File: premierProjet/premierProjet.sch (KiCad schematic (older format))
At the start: 4 parts, among them J1 Conn_01x02_Male, SW1 Pushbutton

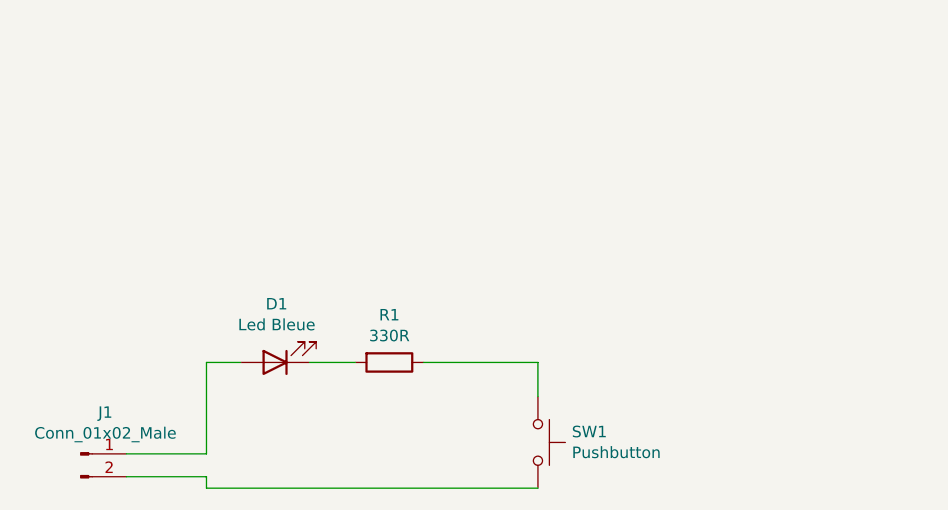
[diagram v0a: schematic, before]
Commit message: Added docs+ /docs
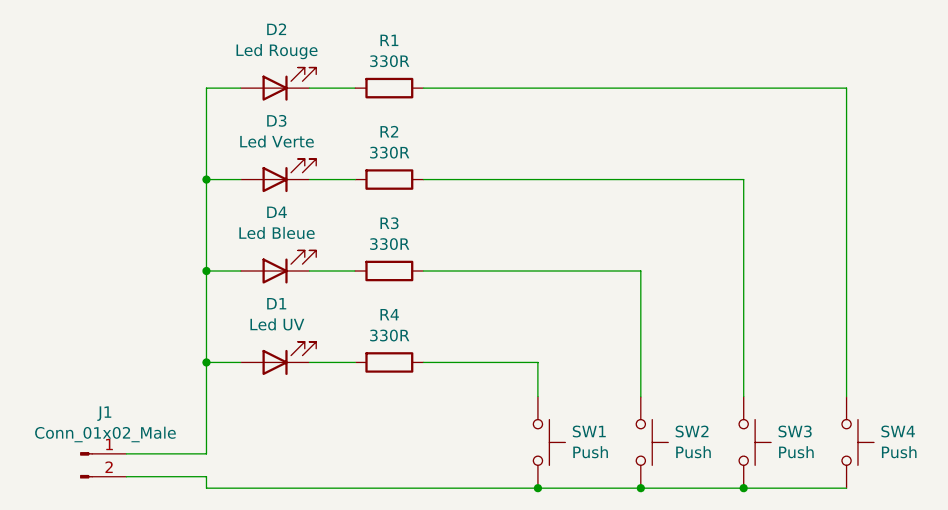
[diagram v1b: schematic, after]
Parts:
- added D2: Led Rouge, symbol Device:LED
- added D3: Led Verte, symbol Device:LED
- added D4: Led Bleue, symbol Device:LED
- added R1, R2, R3: 330R, symbol Device:R
- added SW2, SW3, SW4: Push, symbol Switch:SW_Push
- D1: value Led Bleue -> Led UV
- SW1: value Pushbutton -> Push
- renumbered R1 to R4
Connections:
- net at D1.2 (A), J1.1 (Pin_1): now also D2.2 (A), D3.2 (A), D4.2 (A)
- net at J1.2 (Pin_2), SW1.2: now also SW2.2, SW3.2, SW4.2
- new net: D4.1 (K), R3.2
- new net: R3.1, SW2.1
- new net: D3.1 (K), R2.2
- new net: R2.1, SW3.1
- new net: D2.1 (K), R1.2
- new net: R1.1, SW4.1
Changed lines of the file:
@@
 P 4350 3500
 F 0 "D1" H 4343 3245 50  0000 C CNN
-F 1 "Led Bleue" H 4343 3336 50  0000 C CNN
+F 1 "Led UV" H 4343 3336 50  0000 C CNN
 F 2 "" H 4350 3500 50  0001 C CNN
 F 3 "~" H 4350 3500 50  0001 C CNN
@@
 $EndComp
 $Comp
-L Device:R R1
+L Device:R R4
 U 1 1 5EB78021
 P 4850 3500
-F 0 "R1" V 4643 3500 50  0000 C CNN
+F 0 "R4" V 4643 3500 50  0000 C CNN
 F 1 "330R" V 4734 3500 50  0000 C CNN
 F 2 "" V 4780 3500 50  0001 C CNN
@@
 P 5500 3850
 F 0 "SW1" V 5454 3998 50  0000 L CNN
-F 1 "Pushbutton" V 5545 3998 50  0000 L CNN
+F 1 "Push" V 5545 3998 50  0000 L CNN
 F 2 "" H 5500 4050 50  0001 C CNN
 F 3 "~" H 5500 4050 50  0001 C CNN
@@
 Wire Wire Line
 	4050 4000 3700 4000
+$Comp
+L Device:LED D4
+U 1 1 5EB6F771
+P 4350 3100
+F 0 "D4" H 4343 2845 50  0000 C CNN
+F 1 "Led Bleue" H 4343 2936 50  0000 C CNN
+F 2 "" H 4350 3100 50  0001 C CNN
+F 3 "~" H 4350 3100 50  0001 C CNN
+	1    4350 3100
+	-1   0    0    1
+$EndComp
+$Comp
+L Device:R R3
+U 1 1 5EB6F777
+P 4850 3100
+F 0 "R3" V 4643 3100 50  0000 C CNN
+F 1 "330R" V 4734 3100 50  0000 C CNN
+F 2 "" V 4780 3100 50  0001 C CNN
+F 3 "~" H 4850 3100 50  0001 C CNN
+	1    4850 3100
+	0    1    1    0
+$EndComp
+Wire Wire Line
+	4050 3500 4050 3100
+Wire Wire Line
+	4050 3100 4200 3100
+Wire Wire Line
+	4500 3100 4700 3100
+$Comp
+L Device:LED D3
+U 1 1 5EB70A7C
+P 4350 2700
+F 0 "D3" H 4343 2445 50  0000 C CNN
+F 1 "Led Verte" H 4343 2536 50  0000 C CNN
+F 2 "" H 4350 2700 50  0001 C CNN
+F 3 "~" H 4350 2700 50  0001 C CNN
+	1    4350 2700
+	-1   0    0    1
+$EndComp
+$Comp
+L Device:R R2
+U 1 1 5EB70A82
+P 4850 2700
+F 0 "R2" V 4643 2700 50  0000 C CNN
+F 1 "330R" V 4734 2700 50  0000 C CNN
+F 2 "" V 4780 2700 50  0001 C CNN
+F 3 "~" H 4850 2700 50  0001 C CNN
+	1    4850 2700
+	0    1    1    0
+$EndComp
+Wire Wire Line
+	4050 3100 4050 2700
+Wire Wire Line
+	4050 2700 4200 2700
+Wire Wire Line
+	4500 2700 4700 2700
+$Comp
+L Device:LED D2
+U 1 1 5EB71F2C
+P 4350 2300
+F 0 "D2" H 4343 2045 50  0000 C CNN
+F 1 "Led Rouge" H 4343 2136 50  0000 C CNN
+F 2 "" H 4350 2300 50  0001 C CNN
+F 3 "~" H 4350 2300 50  0001 C CNN
+	1    4350 2300
+	-1   0    0    1
+$EndComp
+$Comp
+L Device:R R1
+U 1 1 5EB71F32
+P 4850 2300
+F 0 "R1" V 4643 2300 50  0000 C CNN
+F 1 "330R" V 4734 2300 50  0000 C CNN
+F 2 "" V 4780 2300 50  0001 C CNN
+F 3 "~" H 4850 2300 50  0001 C CNN
+	1    4850 2300
+	0    1    1    0
+$EndComp
+Wire Wire Line
+	4050 2700 4050 2300
+Wire Wire Line
+	4050 2300 4200 2300
+Wire Wire Line
+	4500 2300 4700 2300
+$Comp
+L Switch:SW_Push SW2
+U 1 1 5EB72A41
+P 5950 3850
+F 0 "SW2" V 5904 3998 50  0000 L CNN
+F 1 "Push" V 5995 3998 50  0000 L CNN
+F 2 "" H 5950 4050 50  0001 C CNN
+F 3 "~" H 5950 4050 50  0001 C CNN
+	1    5950 3850
+	0    1    1    0
+$EndComp
+$Comp
+L Switch:SW_Push SW3
+U 1 1 5EB733F4
+P 6400 3850
+F 0 "SW3" V 6354 3998 50  0000 L CNN
+F 1 "Push" V 6445 3998 50  0000 L CNN
+F 2 "" H 6400 4050 50  0001 C CNN
+F 3 "~" H 6400 4050 50  0001 C CNN
+	1    6400 3850
+	0    1    1    0
+$EndComp
+$Comp
+L Switch:SW_Push SW4
+U 1 1 5EB7399B
+P 6850 3850
+F 0 "SW4" V 6804 3998 50  0000 L CNN
+F 1 "Push" V 6895 3998 50  0000 L CNN
+F 2 "" H 6850 4050 50  0001 C CNN
+F 3 "~" H 6850 4050 50  0001 C CNN
+	1    6850 3850
+	0    1    1    0
+$EndComp
+Wire Wire Line
+	5500 4050 5950 4050
+Connection ~ 5500 4050
+Connection ~ 5950 4050
+Wire Wire Line
+	5950 4050 6400 4050
+Connection ~ 6400 4050
+Wire Wire Line
+	6400 4050 6850 4050
+Wire Wire Line
+	5000 3100 5950 3100
+Wire Wire Line
+	5950 3100 5950 3650
+Wire Wire Line
+	5000 2700 6400 2700
+Wire Wire Line
+	6400 2700 6400 3650
+Wire Wire Line
+	5000 2300 6850 2300
+Wire Wire Line
+	6850 2300 6850 3650
+Connection ~ 4050 3500
+Connection ~ 4050 3100
+Connection ~ 4050 2700
 $EndSCHEMATC

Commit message: PCB du prmierProjet
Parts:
- D1, D3: footprint (none) -> LED_SMD:LED_0805_2012Metric_Pad1.15x1.40mm_HandSolder
- D2: renamed from D4; footprint (none) -> LED_SMD:LED_0805_2012Metric_Pad1.15x1.40mm_HandSolder
- D4: renamed from D2; footprint (none) -> LED_SMD:LED_0805_2012Metric_Pad1.15x1.40mm_HandSolder
- J1: footprint (none) -> Connector_PinHeader_2.54mm:PinHeader_1x02_P2.54mm_Horizontal
- R1: renamed from R4; footprint (none) -> Resistor_SMD:R_0805_2012Metric_Pad1.15x1.40mm_HandSolder
- R2: renamed from R3; footprint (none) -> Resistor_SMD:R_0805_2012Metric_Pad1.15x1.40mm_HandSolder
- R3: renamed from R2; footprint (none) -> Resistor_SMD:R_0805_2012Metric_Pad1.15x1.40mm_HandSolder
- R4: renamed from R1; footprint (none) -> Resistor_SMD:R_0805_2012Metric_Pad1.15x1.40mm_HandSolder
- SW1, SW2, SW3, SW4: footprint (none) -> Button_Switch_THT:SW_PUSH_6mm
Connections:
- net Plus: now reaches D1.2 (A), D2.2 (A), D3.2 (A), D4.2 (A), J1.1 (Pin_1)
- net Masse: now reaches J1.2 (Pin_2), SW1.2, SW2.2, SW3.2, SW4.2
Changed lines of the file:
@@
 F 0 "D1" H 4343 3245 50  0000 C CNN
 F 1 "Led UV" H 4343 3336 50  0000 C CNN
-F 2 "" H 4350 3500 50  0001 C CNN
+F 2 "LED_SMD:LED_0805_2012Metric_Pad1.15x1.40mm_HandSolder" H 4350 3500 50  0001 C CNN
 F 3 "~" H 4350 3500 50  0001 C CNN
 	1    4350 3500
@@
 $EndComp
 $Comp
-L Device:R R4
+L Device:R R1
 U 1 1 5EB78021
 P 4850 3500
-F 0 "R4" V 4643 3500 50  0000 C CNN
+F 0 "R1" V 4643 3500 50  0000 C CNN
 F 1 "330R" V 4734 3500 50  0000 C CNN
-F 2 "" V 4780 3500 50  0001 C CNN
+F 2 "Resistor_SMD:R_0805_2012Metric_Pad1.15x1.40mm_HandSolder" V 4780 3500 50  0001 C CNN
 F 3 "~" H 4850 3500 50  0001 C CNN
 	1    4850 3500
@@
 F 0 "J1" H 3608 4081 50  0000 C CNN
 F 1 "Conn_01x02_Male" H 3608 3990 50  0000 C CNN
-F 2 "" H 3500 3900 50  0001 C CNN
+F 2 "Connector_PinHeader_2.54mm:PinHeader_1x02_P2.54mm_Horizontal" H 3500 3900 50  0001 C CNN
 F 3 "~" H 3500 3900 50  0001 C CNN
 	1    3500 3900
@@
 F 0 "SW1" V 5454 3998 50  0000 L CNN
 F 1 "Push" V 5545 3998 50  0000 L CNN
-F 2 "" H 5500 4050 50  0001 C CNN
+F 2 "Button_Switch_THT:SW_PUSH_6mm" H 5500 4050 50  0001 C CNN
 F 3 "~" H 5500 4050 50  0001 C CNN
 	1    5500 3850
@@
 	4050 4000 3700 4000
 $Comp
-L Device:LED D4
+L Device:LED D2
 U 1 1 5EB6F771
 P 4350 3100
-F 0 "D4" H 4343 2845 50  0000 C CNN
+F 0 "D2" H 4343 2845 50  0000 C CNN
 F 1 "Led Bleue" H 4343 2936 50  0000 C CNN
-F 2 "" H 4350 3100 50  0001 C CNN
+F 2 "LED_SMD:LED_0805_2012Metric_Pad1.15x1.40mm_HandSolder" H 4350 3100 50  0001 C CNN
 F 3 "~" H 4350 3100 50  0001 C CNN
 	1    4350 3100
@@
 $EndComp
 $Comp
-L Device:R R3
+L Device:R R2
 U 1 1 5EB6F777
 P 4850 3100
-F 0 "R3" V 4643 3100 50  0000 C CNN
+F 0 "R2" V 4643 3100 50  0000 C CNN
 F 1 "330R" V 4734 3100 50  0000 C CNN
-F 2 "" V 4780 3100 50  0001 C CNN
+F 2 "Resistor_SMD:R_0805_2012Metric_Pad1.15x1.40mm_HandSolder" V 4780 3100 50  0001 C CNN
 F 3 "~" H 4850 3100 50  0001 C CNN
 	1    4850 3100
@@
 F 0 "D3" H 4343 2445 50  0000 C CNN
 F 1 "Led Verte" H 4343 2536 50  0000 C CNN
-F 2 "" H 4350 2700 50  0001 C CNN
+F 2 "LED_SMD:LED_0805_2012Metric_Pad1.15x1.40mm_HandSolder" H 4350 2700 50  0001 C CNN
 F 3 "~" H 4350 2700 50  0001 C CNN
 	1    4350 2700
@@
 $EndComp
 $Comp
-L Device:R R2
+L Device:R R3
 U 1 1 5EB70A82
 P 4850 2700
-F 0 "R2" V 4643 2700 50  0000 C CNN
+F 0 "R3" V 4643 2700 50  0000 C CNN
 F 1 "330R" V 4734 2700 50  0000 C CNN
-F 2 "" V 4780 2700 50  0001 C CNN
+F 2 "Resistor_SMD:R_0805_2012Metric_Pad1.15x1.40mm_HandSolder" V 4780 2700 50  0001 C CNN
 F 3 "~" H 4850 2700 50  0001 C CNN
 	1    4850 2700
@@
 	4500 2700 4700 2700
 $Comp
-L Device:LED D2
+L Device:LED D4
 U 1 1 5EB71F2C
 P 4350 2300
-F 0 "D2" H 4343 2045 50  0000 C CNN
+F 0 "D4" H 4343 2045 50  0000 C CNN
 F 1 "Led Rouge" H 4343 2136 50  0000 C CNN
-F 2 "" H 4350 2300 50  0001 C CNN
+F 2 "LED_SMD:LED_0805_2012Metric_Pad1.15x1.40mm_HandSolder" H 4350 2300 50  0001 C CNN
 F 3 "~" H 4350 2300 50  0001 C CNN
 	1    4350 2300
@@
 $EndComp
 $Comp
-L Device:R R1
+L Device:R R4
 U 1 1 5EB71F32
 P 4850 2300
-F 0 "R1" V 4643 2300 50  0000 C CNN
+F 0 "R4" V 4643 2300 50  0000 C CNN
 F 1 "330R" V 4734 2300 50  0000 C CNN
-F 2 "" V 4780 2300 50  0001 C CNN
+F 2 "Resistor_SMD:R_0805_2012Metric_Pad1.15x1.40mm_HandSolder" V 4780 2300 50  0001 C CNN
 F 3 "~" H 4850 2300 50  0001 C CNN
 	1    4850 2300
@@
 F 0 "SW2" V 5904 3998 50  0000 L CNN
 F 1 "Push" V 5995 3998 50  0000 L CNN
-F 2 "" H 5950 4050 50  0001 C CNN
+F 2 "Button_Switch_THT:SW_PUSH_6mm" H 5950 4050 50  0001 C CNN
 F 3 "~" H 5950 4050 50  0001 C CNN
 	1    5950 3850
@@
 F 0 "SW3" V 6354 3998 50  0000 L CNN
 F 1 "Push" V 6445 3998 50  0000 L CNN
-F 2 "" H 6400 4050 50  0001 C CNN
+F 2 "Button_Switch_THT:SW_PUSH_6mm" H 6400 4050 50  0001 C CNN
 F 3 "~" H 6400 4050 50  0001 C CNN
 	1    6400 3850
@@
 F 0 "SW4" V 6804 3998 50  0000 L CNN
 F 1 "Push" V 6895 3998 50  0000 L CNN
-F 2 "" H 6850 4050 50  0001 C CNN
+F 2 "Button_Switch_THT:SW_PUSH_6mm" H 6850 4050 50  0001 C CNN
 F 3 "~" H 6850 4050 50  0001 C CNN
 	1    6850 3850
@@
 Connection ~ 4050 3100
 Connection ~ 4050 2700
+Text Label 4350 4050 0    50   ~ 0
+Masse
+Text Label 4050 3400 1    50   ~ 0
+Plus
 $EndSCHEMATC
